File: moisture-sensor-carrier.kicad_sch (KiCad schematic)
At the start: 53 parts, among them J1 USB-C receptacle, J2 Battery 103450 + NTC, J3 Solar panel, J4 SWD 10p 1.27mm, J5 Antenna feed, U1 nRF54L15-QFAA, U2 nPM1300-QEAA, U3 FDC1004, X1 32.768kHz CL=9pF 20ppm, X2 32MHz CL=8pF 40ppm

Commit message: Add SHT45-AD1F ambient RH/T sensor
Primarily a compensation input, not a feature: water permittivity falls
~0.4 %/C, which on a 5-15 pF soil reading is 20-60 fF/C - about 100x the
FDC1004's own 0.28 fF/C offset drift. Without ambient temperature you
cannot separate wetter soil from a warmer room.

That makes T accuracy the deciding spec, so SHT45 (+/-0.1 C) over SHT40/41
(+/-0.2 C) and definitely over SHT43 (+/-0.48 C, which would make
temperature the dominant moisture error). RH accuracy is near-irrelevant
by comparison.

Sits on always-on +3V3, NOT the gated FDC_VDD: Table 6 rates every pin at
VSS-0.3..VDD+0.3 with no independent I/O rating, so gating it while the
bus pull-ups are high violates abs max every sleep cycle. Exactly the
opposite of the FDC1004, whose SCL/SDA are rated 6 V regardless of VDD.
Costs 80 nA idle, ~0.7 mAh/yr.

Uses the _NoCentralPad footprint: Sensirion require the die pad NOT be
soldered and no copper under the sensor, or the internal heater is
thermally shorted.

I2C addresses confirmed distinct: FDC1004 0x50, nPM1300 0x6B, SHT45 0x44.

ERC: 0 errors, 0 warnings.

Co-Authored-By: Claude Opus 5 <noreply@anthropic.com>
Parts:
- added C27: 100nF X7R, symbol Device:C_Small
- added U4: SHT45-AD1F, Sensor_Humidity:Sensirion_DFN-4_1.5x1.5mm_P0.8mm_SHT4x_NoCentralPad, symbol sht4x:SHT4x
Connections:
- net +3V3: now also C27.1, U4.3 (VDD)
- net GND: now also C27.2, U4.4 (VSS)
- net SCL: now also U4.2 (SCL)
- net SDA: now also U4.1 (SDA)

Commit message: Correct MCU support circuit against Nordic QFAA reference layout 0.8
The reference layout package exposed four real errors in the support
circuitry, all of which were plausible-looking but wrong:

- DCC -> L1 -> DECD, then DECD -> FB1 -> DECA. I had L1 feeding VDD and
  FB1 in series with the supply rail. Different circuit entirely.
- DECRF (33) is the SAME NET as DECA (43), not separately decoupled. The
  C14 100nF I had invented is not in Nordic's BOM.
- C13 3.9pF is the RESET filter cap, not an RF matching component. It is
  drawn next to the matching network on Nordic's sheet, which is how it
  ended up in the RF chain. The chain ends at the C11 shunt.
- C5 2.2nF belongs on DECA, not on RESET.

Net-by-net diff against the reference now matches on all of DCC, DECD,
DECA, NRESET, ANT, RF_A, RF_B and ANT_FEED.

VDD (10,22,36,47,48) now goes straight to +3V3; the +3V3_MCU net is gone.

ERC: 0 errors, 0 warnings.

Co-Authored-By: Claude Opus 5 <noreply@anthropic.com>
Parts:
- removed C14: 100nF X7R, symbol Device:C_Small
- C3: value 10uF/6.3V X6S -> 10uF/6.3V X6S 0402
- L1: value 4.7uH 120mA DCC -> 4.7uH 120mA 0603
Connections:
- net DECRF is gone; now on net DECA: U1.33 (DECRF)
- net +3V3: now also C10.1, C3.1, C4.1, C7.1, C8.1, J4.1 (Pin_1), U1.10 (VDD), U1.22 (VDD), U1.36 (VDD), U1.47 (VDD), U1.48 (VDD); no longer FB1.1
- net ANT_FEED: now also C11.1, L4.2; no longer C13.2
- net DECA: now also C2.1, C5.1, FB1.2; no longer C1.1
- net DECD: now also C1.1, FB1.1, L1.2; no longer C2.1
- net GND: now also C13.2
- net NRESET: now also C13.1; no longer C5.1
- removed net +3V3_MCU: C10.1, C3.1, C4.1, C7.1, C8.1, FB1.2, J4.1 (Pin_1), L1.2, U1.10 (VDD), U1.22 (VDD), U1.36 (VDD), U1.47 (VDD), U1.48 (VDD)
- removed net RF_C: C11.1, C13.1, L4.2

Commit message: Fix pin assignment against nRF54L15 datasheet; NTC now fitted
Datasheet v1.0 invalidated two of the three signal assignments:

- TWIM SCL MUST be on a dedicated clock pin (Table 77). P1.09 is not one.
  Moved SCL to P1.11 (pin 39); QFAA clock pins are P0.03/04, P1.03/04/08/
  11/12, P2.01/06. SDA moved to the physically adjacent pin 38 because the
  datasheet requires the data signal near the clock pin for delay matching.
- PMIC_INT was on P2.00, but Table 40 says P2 cannot wake the system and
  has no SENSE/DETECT or GPIOTE - it could never have woken the MCU from
  System OFF. Moved to P0.00 in the low-power domain.
- Also: peripherals cannot mix pins across ports, so SDA/SCL are both P1.

Battery pack turns out to be DW01P + 8205A with NO thermistor, so TH1 is
now fitted rather than DNP, and must be thermally coupled to the cell -
the nPM1300 requires a thermal protection path.

LFXO INTCAP step size corrected to 0.65 pF (was 0.5 pF from a web source);
range is 3-18 pF. HFXO 4.0-17.0 pF in 0.25 pF steps confirmed. Both
registers take a computed value from per-device FICR trim, not raw pF.

ERC: 0 errors, 0 warnings.

Co-Authored-By: Claude Opus 5 <noreply@anthropic.com>
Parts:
- TH1: value 10k B3435 DNP if pack has NTC -> 10k B3435 - couple to cell; now fitted
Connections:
- net PMIC_INT: now also U1.23 (P0.00); no longer U1.11 (P2.00/SPI.DCX)
- net SCL: now also U1.39 (P1.11/AIN4); no longer U1.37 (P1.09/TAMPC)
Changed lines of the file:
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@@
-		(stroke (width 0) (type default))
-	)
-	(wire (pts (xy 388.62 86.36) (xy 383.54 86.36))
 		(stroke (width 0) (type default))
 	)
@@
 		(stroke (width 0) (type default))
 	)
+	(wire (pts (xy 388.62 116.84) (xy 383.54 116.84))
+		(stroke (width 0) (type default))
+	)
 	(wire (pts (xy 520.7 121.92) (xy 525.7800000000001 121.92))
 		(stroke (width 0) (type default))
@@
 		(stroke (width 0) (type default))
 	)
-	(wire (pts (xy 520.7 91.44) (xy 525.7800000000001 91.44))
-		(stroke (width 0) (type default))
-	)
 	(wire (pts (xy 520.7 88.9) (xy 525.7800000000001 88.9))
+		(stroke (width 0) (type default))
+	)
+	(wire (pts (xy 520.7 86.36) (xy 525.7800000000001 86.36))
 		(stroke (width 0) (type default))
 	)
@@
 	(no_connect (at 388.62 78.74000000000001))
 	(no_connect (at 388.62 81.28))
+	(no_connect (at 388.62 86.36))
 	(no_connect (at 388.62 88.9))
 	(no_connect (at 388.62 91.44))
@@
 	(no_connect (at 388.62 109.22))
 	(no_connect (at 388.62 111.75999999999999))
-	(no_connect (at 388.62 116.84))
 	(no_connect (at 388.62 119.38))
 	(no_connect (at 520.7 116.84))
 	(no_connect (at 520.7 114.30000000000001))
 	(no_connect (at 520.7 111.75999999999999))
-	(no_connect (at 520.7 86.36))
+	(no_connect (at 520.7 91.44))
 	(no_connect (at 520.7 83.82))
 	(no_connect (at 520.7 81.28))
@@
 		(effects (font (size 1.27 1.27)) (justify right bottom))
 	)
-	(label "PMIC_INT"
-		(at 383.54 86.36 0)
-		(fields_autoplaced yes)
-		(effects (font (size 1.27 1.27)) (justify right bottom))
-	)
 	(label "P2.07_SWO"
 		(at 383.54 104.14 0)
@@
 		(effects (font (size 1.27 1.27)) (justify right bottom))
 	)
+	(label "PMIC_INT"
+		(at 383.54 116.84 0)
+		(fields_autoplaced yes)
+		(effects (font (size 1.27 1.27)) (justify right bottom))
+	)
 	(label "SWDIO"
 		(at 525.7800000000001 121.92 180)
@@
 		(effects (font (size 1.27 1.27)) (justify left bottom))
 	)
-	(label "SCL"
-		(at 525.7800000000001 91.44 180)
-		(fields_autoplaced yes)
-		(effects (font (size 1.27 1.27)) (justify left bottom))
-	)
 	(label "SDA"
 		(at 525.7800000000001 88.9 180)
+		(fields_autoplaced yes)
+		(effects (font (size 1.27 1.27)) (justify left bottom))
+	)
+	(label "SCL"
+		(at 525.7800000000001 86.36 180)
 		(fields_autoplaced yes)
 		(effects (font (size 1.27 1.27)) (justify left bottom))
@@
 		(in_bom yes)
 		(on_board yes)
-		(dnp yes)
+		(dnp no)
 		(fields_autoplaced yes)
 		(property "Reference" "TH1"
@@
 			(effects (font (size 1.27 1.27)) (justify left))
 		)
-		(property "Value" "10k B3435 DNP if pack has NTC"
+		(property "Value" "10k B3435 - couple to cell"
 			(at 60.96 220.98 0)
 			(effects (font (size 1.27 1.27)) (justify left))

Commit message: Assign footprints to all 54 components; add BOM.md
Hand-solder variants throughout, except the RF matching network (L2/L3/L4/
C6/C9/C11) which stays 0201 standard - Nordic's values are matched to their
reference land pattern and hand-solder pads shift a 0.3pF cap at 2.4GHz.
MCU support passives moved from Nordic's 0201 to 0402 for assembly.

Two symbol corrections found while assigning:
- X1 was a 4-pin Crystal_GND24_Small, but 32.768kHz 2012 parts are 2-pin
  and only 2-pin 2012 footprints exist. Now Crystal_Small.
- J1 was the 24-pin USB_C_Receptacle; swapped to USB_C_Receptacle_USB2.0_16P
  to match the HRO TYPE-C-31-M-12 footprint.

Crystal constraints from datasheet 11.9.1/11.9.2: C_L is capped at 9pF on
both oscillators, which rules out the common 12.5pF 32.768kHz parts. LFXO
drive level max 0.5uW. HFXO BLE tolerance is +/-40ppm, LFXO +/-500ppm.
ESR is a curve against C0, not a single number.

Still unselected: crystals (ordering codes), L1, D5, and the solar
pre-regulator. BOM.md lists requirements and candidates for each.

ERC: 0 errors, 0 warnings.

Co-Authored-By: Claude Opus 5 <noreply@anthropic.com>
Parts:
- removed X1: 32.768kHz CL=9pF 20ppm, symbol Device:Crystal_GND24_Small
- added X1: 32.768kHz CL=9pF 20ppm, Crystal:Crystal_SMD_2012-2Pin_2.0x1.2mm_HandSoldering, symbol Device:Crystal_Small
- C1, C10, C12, C13, C2, C25, C26, C27, C4, C5, C7, C8: footprint (none) -> Capacitor_SMD:C_0402_1005Metric_Pad0.74x0.62mm_HandSolder
- C11, C6, C9: footprint (none) -> Capacitor_SMD:C_0201_0603Metric
- C20, C21, C22, C23, C24, C3: footprint (none) -> Capacitor_SMD:C_0603_1608Metric_Pad1.08x0.95mm_HandSolder
- D3, D4: footprint (none) -> LED_SMD:LED_0603_1608Metric_Pad1.05x0.95mm_HandSolder
- D5: footprint (none) -> Diode_SMD:D_SOD-323_HandSoldering
- FB1: footprint (none) -> Inductor_SMD:L_0402_1005Metric_Pad0.77x0.64mm_HandSolder
- J1: footprint (none) -> Connector_USB:USB_C_Receptacle_HRO_TYPE-C-31-M-12
- J2: footprint (none) -> Connector_JST:JST_PH_B3B-PH-K_1x03_P2.00mm_Vertical
- J3: footprint (none) -> Connector_JST:JST_PH_B2B-PH-K_1x02_P2.00mm_Vertical
- J4: footprint (none) -> Connector_PinHeader_1.27mm:PinHeader_2x05_P1.27mm_Vertical_SMD
- J5, TP1, TP2, TP3, TP4, TP5: footprint (none) -> TestPoint:TestPoint_Pad_D1.0mm
- L1: footprint (none) -> Inductor_SMD:L_0603_1608Metric_Pad1.05x0.95mm_HandSolder
- L10: footprint (none) -> Inductor_SMD:L_Murata_DFE201610P
- L2, L3, L4: footprint (none) -> Inductor_SMD:L_0201_0603Metric
- R1, R20, R21, R22, R23, R25, R26: footprint (none) -> Resistor_SMD:R_0402_1005Metric_Pad0.72x0.64mm_HandSolder
- TH1: footprint (none) -> Resistor_SMD:R_0603_1608Metric_Pad0.98x0.95mm_HandSolder
- X2: footprint (none) -> Crystal:Crystal_SMD_2016-4Pin_2.0x1.6mm
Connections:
- net XL1: now also X1.1
- net XL2: now also X1.2

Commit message: Net-tie the RF grounds; swap J2/J3/J4 for the height budget
Both changes land in tools_gen_sch.py. ERC 0/0, DRC 0/0.

RF grounding. Nordic requires C6 to ground only at pin 32 (VSS_PA) on the
top layer with pin 32 reaching pin 49 only under the package, and C9 to
ground only on the bottom layer. Electrically one node, so invisible in a
netlist. Split into /GND_PA (C6.2, U1.32) and /GND_C9 (C9.2), rejoined by
NT1 and NT2. Three DRU rules enforce the routing half - verified by
injecting illegal geometry and confirming each fires. The placement half
(NT1 under U1 on F.Cu, NT2 on B.Cu) goes in tools_gen_pcb.py.

/GND_PA carries a PWR_FLAG: U1 pin 32 is a power input and splitting it
off GND left it with only passive pins.

Connectors. The 1551WK leaves 6.70 mm under the cell; JST PH is 8 mm
mounting height and the 2x5 1.27 mm header comparable. J2/J3 to JST GH
(~4.7 mm, 1 A), J4 to Tag-Connect TC2050-IDC-NL (zero height, same 10-pin
Cortex pinout, no net changes).

Also: both generators now derive PROJ from __file__. The hardcoded path in
tools_gen_sch.py wrote into the main working tree when run from a worktree.

Co-Authored-By: Claude Opus 5 <noreply@anthropic.com>
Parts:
- added NT1: GND_PA to GND (under U1, F.Cu), NetTie:NetTie-2_SMD_Pad0.5mm, symbol Device:NetTie_2
- added NT2: GND_C9 to GND (B.Cu only), NetTie:NetTie-2_SMD_Pad0.5mm, symbol Device:NetTie_2
- J2: value Battery 103450 + NTC -> Battery 503450 + NTC; footprint Connector_JST:JST_PH_B3B-PH-K_1x03_P2.00mm_Vertical -> Connector_JST:JST_GH_BM03B-GHS-TBT_1x03-1MP_P1.25mm_Vertical
- J3: footprint Connector_JST:JST_PH_B2B-PH-K_1x02_P2.00mm_Vertical -> Connector_JST:JST_GH_BM02B-GHS-TBT_1x02-1MP_P1.25mm_Vertical
- J4: footprint Connector_PinHeader_1.27mm:PinHeader_2x05_P1.27mm_Vertical_SMD -> Connector:Tag-Connect_TC2050-IDC-NL_2x05_P1.27mm_Vertical
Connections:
- net GND: now also NT1.2, NT2.2; no longer C6.2, C9.2, U1.32 (VSS_PA)
- new net GND_C9: C9.2, NT2.1
- new net GND_PA: C6.2, NT1.1, U1.32 (VSS_PA)

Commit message: Place all 56 components; probe electrodes; USB-C edge mount
ERC 0/0. DRC: 0 errors, 4 isolated-copper warnings and 128 unconnected
items, all of which are "nothing is routed yet".

tools_gen_pcb.py now imports the exported netlist and places from a table,
so the board cannot drift from the schematic. It asserts and aborts on:
courtyard overlap, board-edge clearance, mounting-screw clearance, nothing
but AE1 in Zone A, both net-tie placement rules, and SENSE-to-SWITCH
separation. Six real collisions were caught and fixed this way.

Zoning per LAYOUT.md 4 and 6: RF chain in a column at x=16.8 straight up
from U1 pin 31 to the antenna feed, U1 rotated 90 so ANT faces Zone A,
nPM1300 SW2 loop at the bottom, U3 hard against the Zone C boundary and
7.6 mm from U2.

NT1 needed a project footprint. The gap between U1's pin-32 land and the
centre pad is 0.1905 mm and a stock 0.5 mm net tie does not fit; two pads
plus 0.127 mm clearance each side needs 0.254 mm, so the tie also needs a
scoped clearance exemption. Without the net split this would simply be one
net and one piece of copper.

J1 was facing into the board: the HRO footprint mates toward +Y, so it
needs 270 deg, not 90. Now overhangs the left edge by 0.2 mm with its pads
checked on-board and its silk moved to Fab.

Probe electrodes added as filled F.Cu zones, SENSE1 and SENSE2 identical
at 16 x 30 mm, guard pouring around them at 0.2 mm.

Two toolchain notes recorded in LAYOUT.md: DRU rules are last-match-wins
(the net-tie exemption silently did nothing until moved below the fab
minimums), and both Nordic QFN footprints carry their pin-1 marker twice.

Co-Authored-By: Claude Opus 5 <noreply@anthropic.com>
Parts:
- NT1: footprint NetTie:NetTie-2_SMD_Pad0.5mm -> footprints:NetTie_VSSPA
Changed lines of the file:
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@@
 			(effects (font (size 1.27 1.27)) (justify left))
 		)
-		(property "Footprint" "NetTie:NetTie-2_SMD_Pad0.5mm"
+		(property "Footprint" "footprints:NetTie_VSSPA"
 			(at 368.3 370.84 0)
 			(effects (font (size 1.27 1.27)) (hide yes))

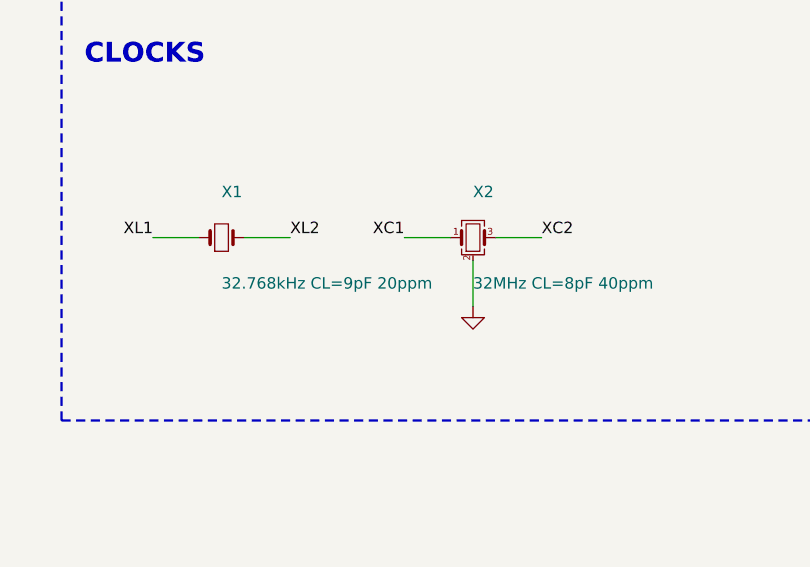
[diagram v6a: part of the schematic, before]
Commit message: X1 = CM8V-T1A 7pF; horizontal connectors; 3D models and enclosure
X1 selected: Micro Crystal CM8V-T1A 32.768 kHz, CL 7 pF, +/-20 ppm.
Checked against every line of the nRF54L15 LFXO table (11.9.2): CL 7 pF
in a 6-9 window, C0 1.2 against typ 1.0 max 2.0, RS 55/70 kOhm against
typ 60 max 100, drive 0.5 uW exactly matched, tolerance +/-20 ppm against
a +/-500 ppm BLE requirement. 7 pF beats the 9 pF the reference BOM
suggested - 9 sits at the hard maximum, 7 sits mid-window with room for
PCB stray either side.

Using Micro Crystal's own land pattern. KiCad's generic 2012 footprints
do not match the datasheet: handsolder is 1.05 mm pads on 1.85 mm centres
and nominal is 0.6 on 1.4, against the specified 0.8 on 1.5.

J2/J3 to side-entry JST GH. Both orientations are the same height (4.20
vs 4.25 mm, measured from the vendor STEP) on an identical board
footprint, so this is about cable exit: the cell hangs from the lid to
within 6.70 mm of the board and a vertical header sends the lead straight
up into it.

3D: wired up the USB-C and SHT45 models, the CM8V-T1A model, and the
Hammond 1551WK enclosure as a mechanical-only footprint so the fit can be
checked in the viewer. All three hand-added vendor models are Y-up CAD
exports and carry a -90 deg X rotation; the enclosure also needs +90 about
Z to line its 80 mm length up with the board. Renders correctly, but the
rotations are inferred from bounding boxes and want eyeballing.

Also: attach_model now clears whatever the footprint shipped with, so J1
and U4 no longer stack a broken KiCad reference under the working one.

Co-Authored-By: Claude Opus 5 <noreply@anthropic.com>
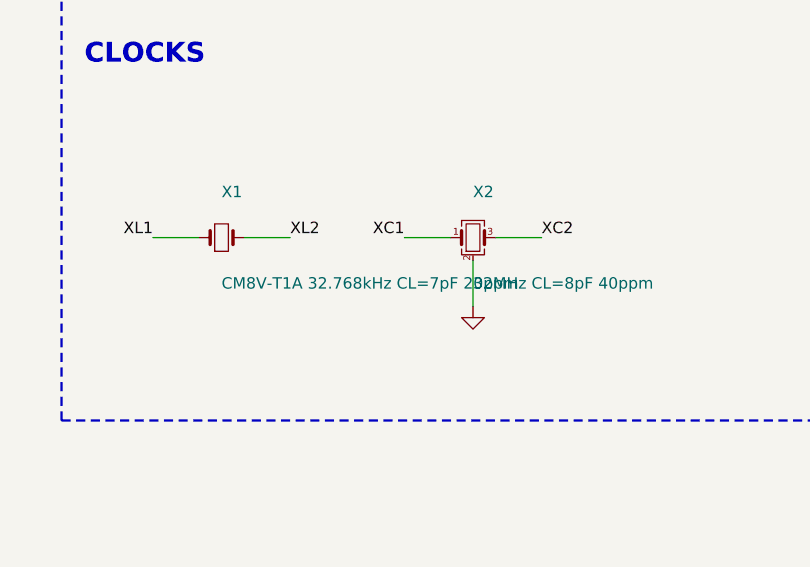
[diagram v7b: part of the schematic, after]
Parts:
- J2: footprint Connector_JST:JST_GH_BM03B-GHS-TBT_1x03-1MP_P1.25mm_Vertical -> Connector_JST:JST_GH_SM03B-GHS-TB_1x03-1MP_P1.25mm_Horizontal
- J3: footprint Connector_JST:JST_GH_BM02B-GHS-TBT_1x02-1MP_P1.25mm_Vertical -> Connector_JST:JST_GH_SM02B-GHS-TB_1x02-1MP_P1.25mm_Horizontal
- X1: value 32.768kHz CL=9pF 20ppm -> CM8V-T1A 32.768kHz CL=7pF 20ppm; footprint Crystal:Crystal_SMD_2012-2Pin_2.0x1.2mm_HandSoldering -> footprints:XTAL_CM8V-T1A_2012
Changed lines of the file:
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@@
 			(effects (font (size 1.27 1.27)) (justify left))
 		)
-		(property "Footprint" "Connector_JST:JST_GH_BM02B-GHS-TBT_1x02-1MP_P1.25mm_Vertical"
+		(property "Footprint" "Connector_JST:JST_GH_SM02B-GHS-TB_1x02-1MP_P1.25mm_Horizontal"
 			(at 88.9 106.68 0)
 			(effects (font (size 1.27 1.27)) (hide yes))
@@
 			(effects (font (size 1.27 1.27)) (justify left))
 		)
-		(property "Footprint" "Connector_JST:JST_GH_BM03B-GHS-TBT_1x03-1MP_P1.25mm_Vertical"
+		(property "Footprint" "Connector_JST:JST_GH_SM03B-GHS-TB_1x03-1MP_P1.25mm_Horizontal"
 			(at 33.02 215.9 0)
 			(effects (font (size 1.27 1.27)) (hide yes))
@@
 			(effects (font (size 1.27 1.27)) (justify left))
 		)
-		(property "Value" "32.768kHz CL=9pF 20ppm"
+		(property "Value" "CM8V-T1A 32.768kHz CL=7pF 20ppm"
 			(at 175.26 347.98 0)
 			(effects (font (size 1.27 1.27)) (justify left))
 		)
-		(property "Footprint" "Crystal:Crystal_SMD_2012-2Pin_2.0x1.2mm_HandSoldering"
+		(property "Footprint" "footprints:XTAL_CM8V-T1A_2012"
 			(at 175.26 342.9 0)
 			(effects (font (size 1.27 1.27)) (hide yes))

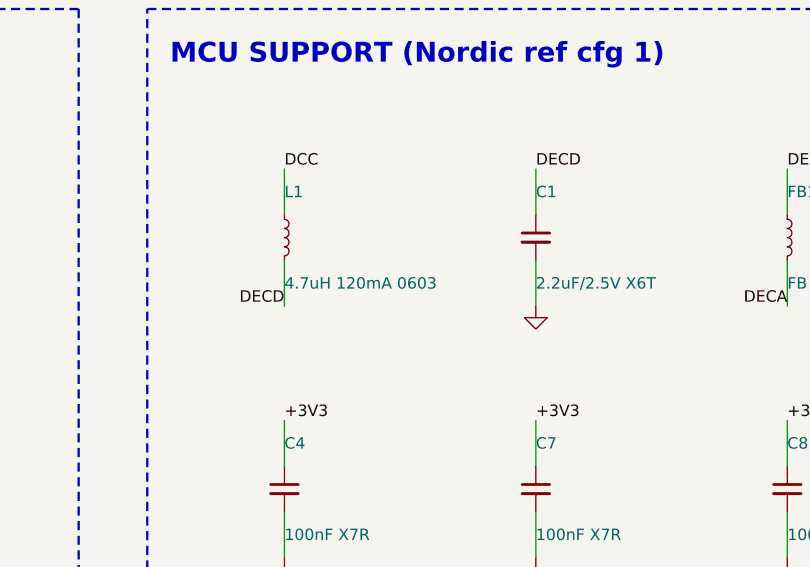
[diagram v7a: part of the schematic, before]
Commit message: L1 = Murata LQM18PN4R7MFRL
Better than the TDK MLZ1608M4R7WT000, which met Nordic's numbers but sat
exactly on two of them. DCR 0.44 Ohm +/-25% gives 550 mOhm worst case
against the 650 mOhm limit, where the TDK's 0.5 +/-30% lands on 650
exactly.

Caveat recorded in BOM.md: the two current figures are not the same
measurement. TDK publishes a saturation current (120 mA at 50% L drop)
and a thermal one (350 mA); Murata's reference spec publishes only a
40 C temperature-rise rating of 620 mA and states no saturation current
at all. The Murata's headroom against Nordic's 120 mA is very likely much
better but this document does not confirm it - get the DC-bias curve from
the full datasheet or SimSurfing before volume.

Also noted: the document is stamped Reference Only, and DCR is not worth
optimising for power here - at a few mA the 100 mOhm difference is
microwatts against a wake cycle that is 0.6% of the budget. The reason to
prefer it is spec margin.

Co-Authored-By: Claude Opus 5 <noreply@anthropic.com>
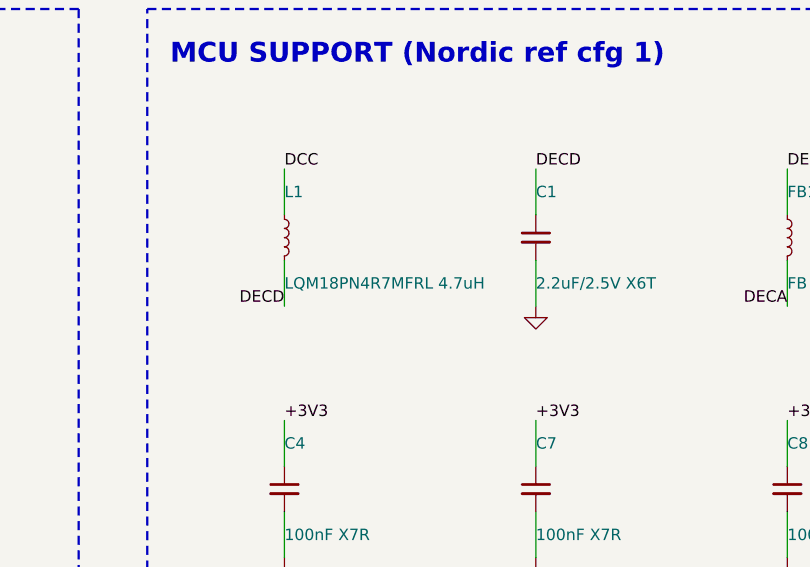
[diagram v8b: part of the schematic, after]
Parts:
- L1: value 4.7uH 120mA 0603 -> LQM18PN4R7MFRL 4.7uH
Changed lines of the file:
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@@
 			(effects (font (size 1.27 1.27)) (justify left))
 		)
-		(property "Value" "4.7uH 120mA 0603"
+		(property "Value" "LQM18PN4R7MFRL 4.7uH"
 			(at 368.3 220.98 0)
 			(effects (font (size 1.27 1.27)) (justify left))
